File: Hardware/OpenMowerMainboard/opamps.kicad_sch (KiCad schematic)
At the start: 16 parts, among them IC2 TSC101CILT, U2 MCP604

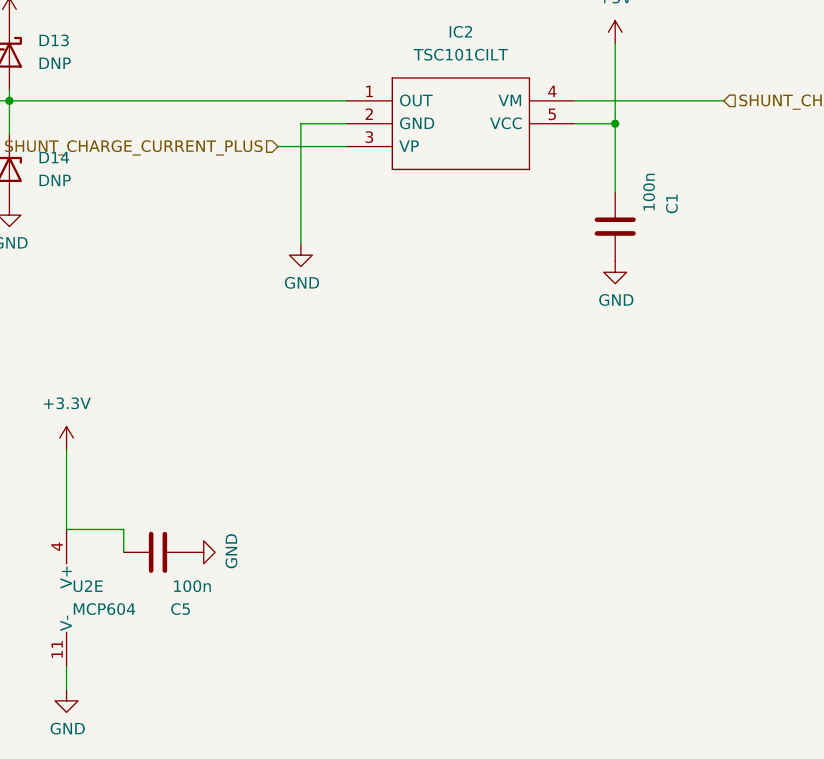
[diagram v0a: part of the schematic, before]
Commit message: BoM data added to kicad - results exported to .xlsx file
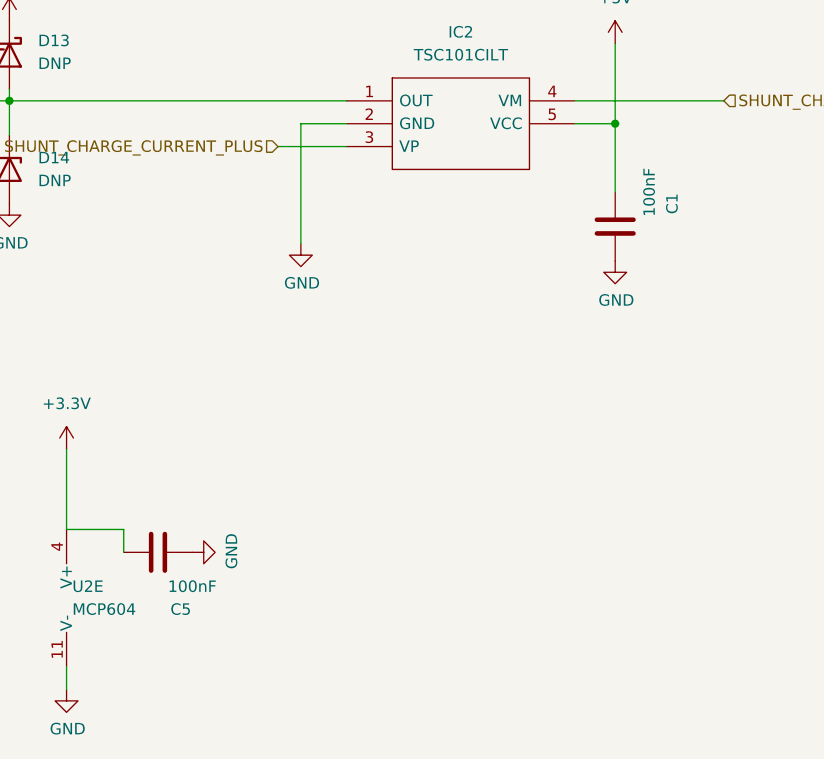
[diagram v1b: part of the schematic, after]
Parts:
- C1, C5: value 100n -> 100nF; Digikey (none) -> 490-4789-1-ND; Part Number (none) -> GCM21BR72A104KA37L; Stock_PN (none) -> C-805-.1uF-100V-X7R
- D13, D14, TP1, TP2, TP5: Config (none) -> do not place
- IC2: Digikey (none) -> 497-6947-1-ND; Part Number (none) -> TSC101CILT; Stock_PN (none) -> U-TSC101CILT
- R44, R46: Digikey (none) -> 311-47.0KCRCT-ND; Part Number (none) -> RC0805FR-0747KL; Stock_PN (none) -> R-805-47K-.125W-1%
- R45, R47: Digikey (none) -> 311-1.00KCRCT-ND; Part Number (none) -> RC0805FR-071KL; Stock_PN (none) -> R-805-1K-.125W-1%
- R48, R50: Digikey (none) -> 738-RMCF0805FG10K0CT-ND; Part Number (none) -> RMCF0805FG10K0; Stock_PN (none) -> R-805-10K-.125W-1%
- R49: Digikey (none) -> 311-4.70KCRCT-ND; Part Number (none) -> RC0805FR-074K7L; Stock_PN (none) -> R-805-4.7K-.125W-1%
- U2: Digikey (none) -> MCP604T-E/SLCT-ND; Part Number (none) -> MCP604T-E/SL; Stock_PN (none) -> U-MCP604T-E/SL
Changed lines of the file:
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@@
     (in_bom yes) (on_board yes)
     (property "Reference" "C5" (id 0) (at 165.735 170.815 90))
-    (property "Value" "100n" (id 1) (at 167.005 168.275 90))
+    (property "Value" "100nF" (id 1) (at 167.005 168.275 90))
     (property "Footprint" "Capacitor_SMD:C_0805_2012Metric_Pad1.18x1.45mm_HandSolder" (id 2) (at 159.385 165.4302 0)
       (effects (font (size 1.27 1.27)) hide)
@@
       (effects (font (size 1.27 1.27)) hide)
     )
+    (property "Digikey" "490-4789-1-ND" (id 4) (at 163.195 164.465 0)
+      (effects (font (size 1.27 1.27)) hide)
+    )
+    (property "Part Number" "GCM21BR72A104KA37L" (id 5) (at 163.195 164.465 0)
+      (effects (font (size 1.27 1.27)) hide)
+    )
+    (property "Stock_PN" "C-805-.1uF-100V-X7R" (id 6) (at 163.195 164.465 0)
+      (effects (font (size 1.27 1.27)) hide)
+    )
     (pin "1")
     (pin "2")
@@
     )
     (property "Datasheet" "~" (id 3) (at 146.685 121.92 0)
+      (effects (font (size 1.27 1.27)) hide)
+    )
+    (property "Config" "do not place" (id 4) (at 146.685 121.92 0)
       (effects (font (size 1.27 1.27)) hide)
     )
@@
     )
     (property "Datasheet" "~" (id 3) (at 149.225 114.3 0)
+      (effects (font (size 1.27 1.27)) hide)
+    )
+    (property "Config" "do not place" (id 4) (at 144.145 114.3 0)
       (effects (font (size 1.27 1.27)) hide)
     )
@@
       (effects (font (size 1.27 1.27)) hide)
     )
+    (property "Digikey" "MCP604T-E/SLCT-ND" (id 4) (at 87.63 127 0)
+      (effects (font (size 1.27 1.27)) hide)
+    )
+    (property "Part Number" "MCP604T-E/SL" (id 5) (at 87.63 127 0)
+      (effects (font (size 1.27 1.27)) hide)
+    )
+    (property "Stock_PN" "U-MCP604T-E/SL" (id 6) (at 87.63 127 0)
+      (effects (font (size 1.27 1.27)) hide)
+    )
     (pin "12")
     (pin "13")
@@
       (effects (font (size 1.27 1.27)) hide)
     )
+    (property "Stock_PN" "R-805-4.7K-.125W-1%" (id 4) (at 100.33 78.74 0)
+      (effects (font (size 1.27 1.27)) hide)
+    )
+    (property "Digikey" "311-4.70KCRCT-ND" (id 5) (at 100.33 78.74 0)
+      (effects (font (size 1.27 1.27)) hide)
+    )
+    (property "Part Number" "RC0805FR-074K7L" (id 6) (at 100.33 78.74 0)
+      (effects (font (size 1.27 1.27)) hide)
+    )
     (pin "1")
     (pin "2")
@@
       (effects (font (size 1.27 1.27)) hide)
     )
+    (property "Digikey" "MCP604T-E/SLCT-ND" (id 4) (at 74.93 67.31 0)
+      (effects (font (size 1.27 1.27)) hide)
+    )
+    (property "Part Number" "MCP604T-E/SL" (id 5) (at 74.93 67.31 0)
+      (effects (font (size 1.27 1.27)) hide)
+    )
+    (property "Stock_PN" "U-MCP604T-E/SL" (id 6) (at 74.93 67.31 0)
+      (effects (font (size 1.27 1.27)) hide)
+    )
     (pin "1")
     (pin "2")
@@
       (effects (font (size 1.27 1.27)) hide)
     )
+    (property "Digikey" "MCP604T-E/SLCT-ND" (id 4) (at 114.3 69.85 0)
+      (effects (font (size 1.27 1.27)) hide)
+    )
+    (property "Part Number" "MCP604T-E/SL" (id 5) (at 114.3 69.85 0)
+      (effects (font (size 1.27 1.27)) hide)
+    )
+    (property "Stock_PN" "U-MCP604T-E/SL" (id 6) (at 114.3 69.85 0)
+      (effects (font (size 1.27 1.27)) hide)
+    )
     (pin "5")
     (pin "6")
@@
       (effects (font (size 1.27 1.27)) hide)
     )
+    (property "Stock_PN" "R-805-1K-.125W-1%" (id 4) (at 92.71 67.31 0)
+      (effects (font (size 1.27 1.27)) hide)
+    )
+    (property "Digikey" "311-1.00KCRCT-ND" (id 5) (at 92.71 67.31 0)
+      (effects (font (size 1.27 1.27)) hide)
+    )
+    (property "Part Number" "RC0805FR-071KL" (id 6) (at 92.71 67.31 0)
+      (effects (font (size 1.27 1.27)) hide)
+    )
     (pin "1")
     (pin "2")
@@
     )
     (property "Datasheet" "~" (id 3) (at 119.38 69.85 0)
+      (effects (font (size 1.27 1.27)) hide)
+    )
+    (property "Config" "do not place" (id 4) (at 124.46 69.85 0)
       (effects (font (size 1.27 1.27)) hide)
     )
@@
       (effects (font (size 1.27 1.27)) hide)
     )
+    (property "Digikey" "MCP604T-E/SLCT-ND" (id 4) (at 87.63 111.125 0)
+      (effects (font (size 1.27 1.27)) hide)
+    )
+    (property "Part Number" "MCP604T-E/SL" (id 5) (at 87.63 111.125 0)
+      (effects (font (size 1.27 1.27)) hide)
+    )
+    (property "Stock_PN" "U-MCP604T-E/SL" (id 6) (at 87.63 111.125 0)
+      (effects (font (size 1.27 1.27)) hide)
+    )
     (pin "10")
     (pin "8")
@@
       (effects (font (size 1.27 1.27)) hide)
     )
+    (property "Digikey" "738-RMCF0805FG10K0CT-ND" (id 4) (at 100.33 58.42 0)
+      (effects (font (size 1.27 1.27)) hide)
+    )
+    (property "Part Number" "RMCF0805FG10K0" (id 5) (at 100.33 58.42 0)
+      (effects (font (size 1.27 1.27)) hide)
+    )
+    (property "Stock_PN" "R-805-10K-.125W-1%" (id 6) (at 100.33 58.42 0)
+      (effects (font (size 1.27 1.27)) hide)
+    )
     (pin "1")
     (pin "2")
@@
       (effects (font (size 1.27 1.27)) hide)
     )
+    (property "Stock_PN" "R-805-47K-.125W-1%" (id 4) (at 49.53 76.2 0)
+      (effects (font (size 1.27 1.27)) hide)
+    )
+    (property "Digikey" "311-47.0KCRCT-ND" (id 5) (at 49.53 76.2 0)
+      (effects (font (size 1.27 1.27)) hide)
+    )
+    (property "Part Number" "RC0805FR-0747KL" (id 6) (at 49.53 76.2 0)
+      (effects (font (size 1.27 1.27)) hide)
+    )
     (pin "1")
     (pin "2")
@@
     )
     (property "Datasheet" "http://ww1.microchip.com/downloads/en/DeviceDoc/21314g.pdf" (id 3) (at 156.845 164.465 0)
+      (effects (font (size 1.27 1.27)) hide)
+    )
+    (property "Digikey" "MCP604T-E/SLCT-ND" (id 4) (at 155.575 169.545 0)
+      (effects (font (size 1.27 1.27)) hide)
+    )
+    (property "Part Number" "MCP604T-E/SL" (id 5) (at 155.575 169.545 0)
+      (effects (font (size 1.27 1.27)) hide)
+    )
+    (property "Stock_PN" "U-MCP604T-E/SL" (id 6) (at 155.575 169.545 0)
       (effects (font (size 1.27 1.27)) hide)
     )
@@
       (effects (font (size 1.27 1.27)) hide)
     )
+    (property "Config" "do not place" (id 4) (at 97.79 67.31 0)
+      (effects (font (size 1.27 1.27)) hide)
+    )
     (pin "1")
   )
@@
       (effects (font (size 1.27 1.27)) hide)
     )
+    (property "Stock_PN" "R-805-47K-.125W-1%" (id 4) (at 74.93 81.28 0)
+      (effects (font (size 1.27 1.27)) hide)
+    )
+    (property "Digikey" "311-47.0KCRCT-ND" (id 5) (at 74.93 81.28 0)
+      (effects (font (size 1.27 1.27)) hide)
+    )
+    (property "Part Number" "RC0805FR-0747KL" (id 6) (at 74.93 81.28 0)
+      (effects (font (size 1.27 1.27)) hide)
+    )
     (pin "1")
     (pin "2")
@@
       (effects (font (size 1.27 1.27)) hide)
     )
+    (property "Digikey" "738-RMCF0805FG10K0CT-ND" (id 4) (at 111.76 53.34 0)
+      (effects (font (size 1.27 1.27)) hide)
+    )
+    (property "Part Number" "RMCF0805FG10K0" (id 5) (at 111.76 53.34 0)
+      (effects (font (size 1.27 1.27)) hide)
+    )
+    (property "Stock_PN" "R-805-10K-.125W-1%" (id 6) (at 111.76 53.34 0)
+      (effects (font (size 1.27 1.27)) hide)
+    )
     (pin "1")
     (pin "2")
@@
       (effects (font (size 1.27 1.27)) hide)
     )
+    (property "Stock_PN" "R-805-1K-.125W-1%" (id 4) (at 59.69 81.28 0)
+      (effects (font (size 1.27 1.27)) hide)
+    )
+    (property "Digikey" "311-1.00KCRCT-ND" (id 5) (at 59.69 81.28 0)
+      (effects (font (size 1.27 1.27)) hide)
+    )
+    (property "Part Number" "RC0805FR-071KL" (id 6) (at 59.69 81.28 0)
+      (effects (font (size 1.27 1.27)) hide)
+    )
     (pin "1")
     (pin "2")
@@
     (in_bom yes) (on_board yes)
     (property "Reference" "C1" (id 0) (at 220.345 125.73 90))
-    (property "Value" "100n" (id 1) (at 217.805 124.46 90))
+    (property "Value" "100nF" (id 1) (at 217.805 124.46 90))
     (property "Footprint" "Capacitor_SMD:C_0805_2012Metric_Pad1.18x1.45mm_HandSolder" (id 2) (at 214.9602 132.08 0)
       (effects (font (size 1.27 1.27)) hide)
     )
     (property "Datasheet" "~" (id 3) (at 213.995 128.27 0)
+      (effects (font (size 1.27 1.27)) hide)
+    )
+    (property "Digikey" "490-4789-1-ND" (id 4) (at 213.995 128.27 0)
+      (effects (font (size 1.27 1.27)) hide)
+    )
+    (property "Part Number" "GCM21BR72A104KA37L" (id 5) (at 213.995 128.27 0)
+      (effects (font (size 1.27 1.27)) hide)
+    )
+    (property "Stock_PN" "C-805-.1uF-100V-X7R" (id 6) (at 213.995 128.27 0)
       (effects (font (size 1.27 1.27)) hide)
     )
@@
       (effects (font (size 1.27 1.27)) (justify left) hide)
     )
+    (property "Digikey" "497-6947-1-ND" (id 10) (at 184.15 114.3 0)
+      (effects (font (size 1.27 1.27)) hide)
+    )
+    (property "Part Number" "TSC101CILT" (id 11) (at 184.15 114.3 0)
+      (effects (font (size 1.27 1.27)) hide)
+    )
+    (property "Stock_PN" "U-TSC101CILT" (id 12) (at 184.15 114.3 0)
+      (effects (font (size 1.27 1.27)) hide)
+    )
     (pin "1")
     (pin "2")
@@
       (effects (font (size 1.27 1.27)) hide)
     )
+    (property "Config" "do not place" (id 4) (at 146.685 109.22 0)
+      (effects (font (size 1.27 1.27)) hide)
+    )

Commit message: BOM changes
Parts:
- D13, D14, TP1, TP2, TP5: DNP (none) -> Y
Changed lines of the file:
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@@
+      (effects (font (size 1.27 1.27)) hide)
+    )
+    (property "DNP" "Y" (id 5) (at 146.685 121.92 0)
       (effects (font (size 1.27 1.27)) hide)
     )
@@
     )
     (property "Config" "do not place" (id 4) (at 144.145 114.3 0)
+      (effects (font (size 1.27 1.27)) hide)
+    )
+    (property "DNP" "Y" (id 5) (at 144.145 114.3 0)
       (effects (font (size 1.27 1.27)) hide)
     )
@@
       (effects (font (size 1.27 1.27)) hide)
     )
+    (property "DNP" "Y" (id 5) (at 124.46 69.85 0)
+      (effects (font (size 1.27 1.27)) hide)
+    )
     (pin "1")
   )
@@
       (effects (font (size 1.27 1.27)) hide)
     )
+    (property "DNP" "Y" (id 5) (at 97.79 67.31 0)
+      (effects (font (size 1.27 1.27)) hide)
+    )
     (pin "1")
   )
@@
       (effects (font (size 1.27 1.27)) hide)
     )
+    (property "DNP" "Y" (id 5) (at 146.685 109.22 0)
+      (effects (font (size 1.27 1.27)) hide)
+    )
